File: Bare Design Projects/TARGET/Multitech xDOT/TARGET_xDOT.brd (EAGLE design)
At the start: 40.5 x 27 mm, 11 parts, among them U1 MTXDOT-EU1-A00-1

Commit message: Added LPC11u35 interface macro
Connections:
- net +3.3V_TGT renamed +3.3V
- net NRESET renamed DAP_NRESET
- net SWCLK renamed DAP_SWCLK
- net SWDIO renamed DAP_SWDIO
- net UART0_RX renamed DAP_RX
- net UART0_TX renamed DAP_TX
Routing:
- added copper zone on layer 16, net +3.3V
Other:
- board outline removed
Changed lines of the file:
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@@
 <board>
 <plain>
-<wire x1="0" y1="0" x2="40.5" y2="0" width="0" layer="20"/>
-<wire x1="40.5" y1="0" x2="40.5" y2="27" width="0" layer="20"/>
-<wire x1="40.5" y1="27" x2="0" y2="27" width="0" layer="20"/>
-<wire x1="0" y1="27" x2="0" y2="0" width="0" layer="20"/>
 <rectangle x1="31.1912" y1="11.3792" x2="40.3352" y2="22.7584" layer="41"/>
 </plain>
@@
 <attribute name="VALUE" x="35.3844" y="22.3428" size="1.016" layer="27" font="vector" ratio="12" rot="R270"/>
 </element>
-<element name="C1" library="mbed-HDK-RLCQ" package="0603" value="10uF" x="2.9845" y="15.7734" rot="R270"/>
+<element name="C1" library="mbed-HDK-RLCQ" package="0603" value="10uF" x="2.9845" y="15.7734" smashed="yes" rot="R270">
+<attribute name="NAME" x="0.7545" y="17.0434" size="1.016" layer="25" font="vector" ratio="12" rot="R270"/>
+<attribute name="VALUE" x="0.4445" y="17.0434" size="1.016" layer="27" font="vector" ratio="12" rot="R270"/>
+</element>
 <element name="C2" library="mbed-HDK-RLCQ" package="0603" value="100nF" x="2.9972" y="19.2151" rot="R90"/>
 <element name="C3" library="mbed-HDK-RLCQ" package="0402" value="6.8pF" x="29.3624" y="21.9456" smashed="yes">
@@
 <contactref element="C7" pad="1"/>
 <polygon width="0.4064" layer="1">
-<vertex x="-12.7" y="50.8"/>
-<vertex x="-12.7" y="-5.08"/>
-<vertex x="49.53" y="-5.08"/>
-<vertex x="49.53" y="50.8"/>
+<vertex x="-64" y="-42.5"/>
+<vertex x="92.5" y="-43"/>
+<vertex x="94" y="68"/>
+<vertex x="-62.5" y="68.5"/>
 </polygon>
 </signal>
@@
 <contactref element="U1" pad="P$14"/>
 </signal>
-<signal name="UART0_TX">
+<signal name="DAP_TX">
 <contactref element="U1" pad="P$15"/>
 </signal>
-<signal name="UART0_RX">
+<signal name="DAP_RX">
 <contactref element="U1" pad="P$16"/>
 </signal>
@@
 <contactref element="U1" pad="P$28"/>
 </signal>
-<signal name="SWCLK">
+<signal name="DAP_SWCLK">
 <contactref element="U1" pad="P$29"/>
 </signal>
-<signal name="SWDIO">
+<signal name="DAP_SWDIO">
 <contactref element="U1" pad="P$30"/>
 </signal>
@@
 <contactref element="U1" pad="P$32"/>
 </signal>
-<signal name="NRESET">
+<signal name="DAP_NRESET">
 <contactref element="U1" pad="P$33"/>
 </signal>
@@
 <signal name="ANT2">
 <contactref element="U1" pad="P$47"/>
-</signal>
-<signal name="+3.3V_TGT">
-<contactref element="U1" pad="P$4"/>
-<contactref element="U1" pad="P$3"/>
-<contactref element="C1" pad="1"/>
-<contactref element="C2" pad="1"/>
-<wire x1="2.9972" y1="18.3651" x2="3.0421" y2="18.41" width="0.508" layer="1"/>
-<wire x1="3.0421" y1="18.41" x2="5.334" y2="18.41" width="0.508" layer="1"/>
-<wire x1="2.9845" y1="16.6234" x2="2.9911" y2="16.63" width="0.508" layer="1"/>
-<wire x1="2.9911" y1="16.63" x2="5.334" y2="16.63" width="0.508" layer="1"/>
-<wire x1="2.9972" y1="18.3651" x2="2.9845" y2="18.3524" width="0.508" layer="1"/>
-<wire x1="2.9845" y1="18.3524" x2="2.9845" y2="16.6234" width="0.508" layer="1"/>
 </signal>
 <signal name="N$4">
@@
 <via x="39.3192" y="9.7536" extent="1-16" drill="0.6"/>
 </signal>
+<signal name="+3.3V">
+<polygon width="0.4064" layer="16">
+<vertex x="-64" y="-43"/>
+<vertex x="92" y="-43"/>
+<vertex x="92" y="68.5"/>
+<vertex x="-64" y="68.5"/>
+</polygon>
+<contactref element="U1" pad="P$4"/>
+<contactref element="U1" pad="P$3"/>
+<contactref element="C1" pad="1"/>
+<contactref element="C2" pad="1"/>
+<wire x1="2.9972" y1="18.3651" x2="3.0421" y2="18.41" width="0.508" layer="1"/>
+<wire x1="3.0421" y1="18.41" x2="5.334" y2="18.41" width="0.508" layer="1"/>
+<wire x1="2.9845" y1="16.6234" x2="2.9911" y2="16.63" width="0.508" layer="1"/>
+<wire x1="2.9911" y1="16.63" x2="5.334" y2="16.63" width="0.508" layer="1"/>
+<wire x1="2.9972" y1="18.3651" x2="2.9845" y2="18.3524" width="0.508" layer="1"/>
+<wire x1="2.9845" y1="18.3524" x2="2.9845" y2="16.6234" width="0.508" layer="1"/>
+</signal>
 </signals>

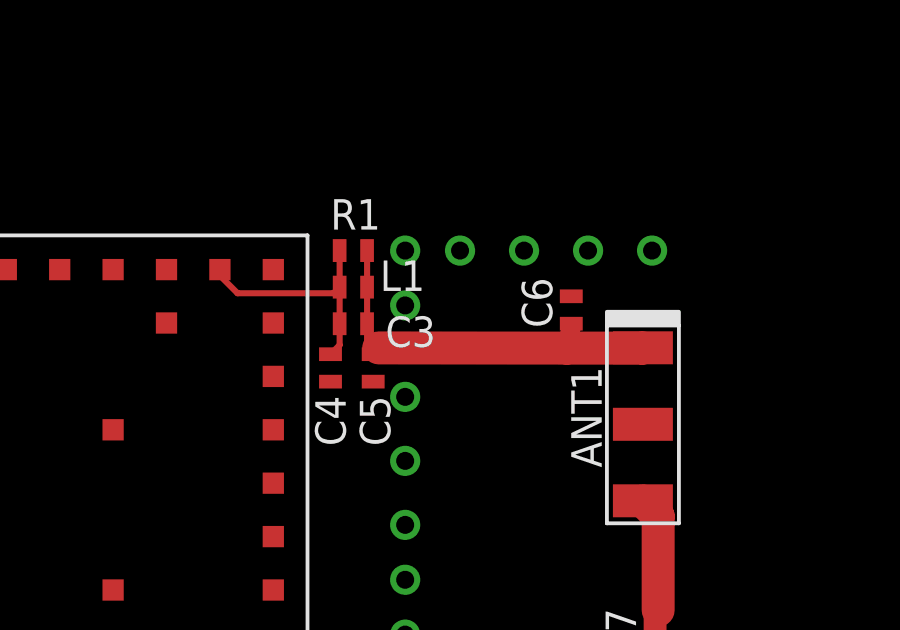
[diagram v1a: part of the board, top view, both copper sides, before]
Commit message: Updated design removed obsolete components
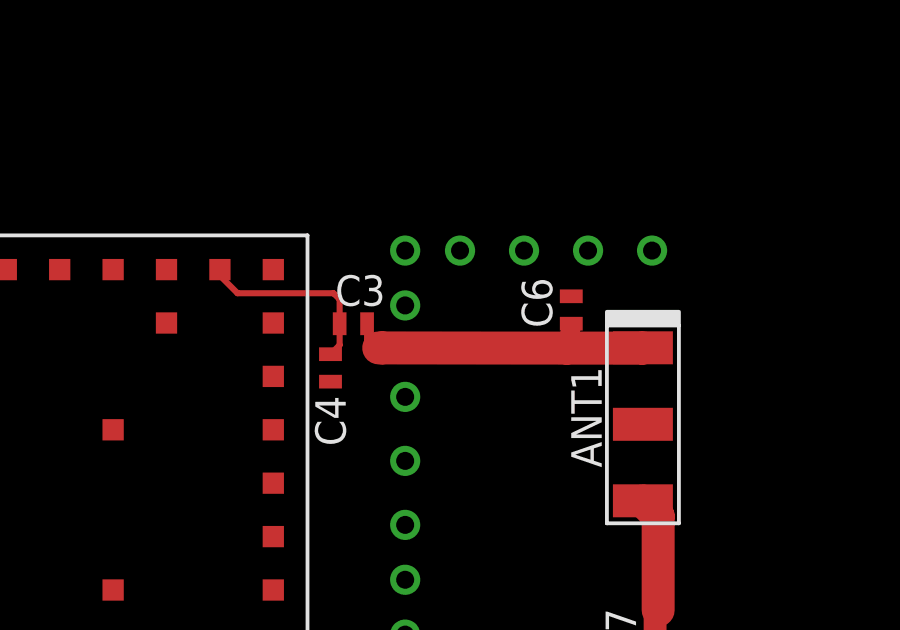
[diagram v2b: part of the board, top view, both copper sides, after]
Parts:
- removed C5: 10pF, mbed-HDK-RLCQ:0402
- removed L1: 7.5uH, mbed-HDK-RLCQ:0402
- removed R1: 0, mbed-HDK-RLCQ:0402
- C3: value 6.8pF -> 9.1pF
- C4: value 10pF -> 5.6pF
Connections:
- net DAP_NRESET renamed TGT_NRESET
- net DAP_SWCLK renamed TGT_SWCLK
- net DAP_SWDIO renamed TGT_SWDIO
- net UART1_RX renamed TGT_RX
- net UART1_TX renamed TGT_TX
- net ANT1: no longer L1.1, R1.1
- net GND: no longer C5.1
- net N$4: no longer C5.2, L1.2, R1.2
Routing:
- net N$4: track 13.7 -> 11.3 mm
- net ANT1: track 8.10 -> 6.47 mm
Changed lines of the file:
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@@
 <setting verticaltext="up"/>
 </settings>
-<grid distance="0.5" unitdist="mm" unit="mm" style="lines" multiple="1" display="no" altdistance="0.00635" altunitdist="mm" altunit="mm"/>
+<grid distance="6" unitdist="mil" unit="mil" style="lines" multiple="1" display="no" altdistance="0.00635" altunitdist="mm" altunit="mm"/>
 <layers>
 <layer number="1" name="Top" color="4" fill="1" visible="yes" active="yes"/>
@@
 </element>
 <element name="C2" library="mbed-HDK-RLCQ" package="0603" value="100nF" x="2.9972" y="19.2151" rot="R90"/>
-<element name="C3" library="mbed-HDK-RLCQ" package="0402" value="6.8pF" x="29.3624" y="21.9456" smashed="yes">
-<attribute name="NAME" x="32.1056" y="22.1869" size="1.016" layer="25" font="vector" ratio="12" rot="R180"/>
+<element name="C3" library="mbed-HDK-RLCQ" package="0402" value="9.1pF" x="29.3624" y="21.9456" smashed="yes">
+<attribute name="NAME" x="30.4292" y="23.5585" size="1.016" layer="25" font="vector" ratio="12" rot="R180"/>
 <attribute name="VALUE" x="28.0924" y="18.1356" size="1.016" layer="27" font="vector" ratio="12"/>
 </element>
-<element name="C4" library="mbed-HDK-RLCQ" package="0402" value="10pF" x="28.6004" y="20.4724" smashed="yes" rot="R90">
+<element name="C4" library="mbed-HDK-RLCQ" package="0402" value="5.6pF" x="28.6004" y="20.4724" smashed="yes" rot="R90">
 <attribute name="NAME" x="29.1084" y="17.8689" size="1.016" layer="25" font="vector" ratio="12" rot="R90"/>
 <attribute name="VALUE" x="32.4104" y="19.2024" size="1.016" layer="27" font="vector" ratio="12" rot="R90"/>
-</element>
-<element name="C5" library="mbed-HDK-RLCQ" package="0402" value="10pF" x="30.0228" y="20.4724" smashed="yes" rot="R90">
-<attribute name="NAME" x="30.5943" y="17.8689" size="1.016" layer="25" font="vector" ratio="12" rot="R90"/>
-<attribute name="VALUE" x="33.8328" y="19.2024" size="1.016" layer="27" font="vector" ratio="12" rot="R90"/>
 </element>
 <element name="C6" library="mbed-HDK-RLCQ" package="0402" value="82pF" x="36.6268" y="22.4028" smashed="yes" rot="R270">
@@
 <attribute name="NAME" x="38.7858" y="10.7823" size="1.016" layer="25" font="vector" ratio="12" rot="R90"/>
 <attribute name="VALUE" x="43.2308" y="10.2108" size="1.016" layer="27" font="vector" ratio="12" rot="R90"/>
-</element>
-<element name="L1" library="mbed-HDK-RLCQ" package="0402" value="7.5uH" x="29.3624" y="23.1648" smashed="yes">
-<attribute name="NAME" x="30.2514" y="23.0378" size="1.016" layer="25" font="vector" ratio="12"/>
-<attribute name="VALUE" x="28.0924" y="19.3548" size="1.016" layer="27" font="vector" ratio="12"/>
-</element>
-<element name="R1" library="mbed-HDK-RLCQ" package="0402" value="0" x="29.3624" y="24.384" smashed="yes">
-<attribute name="NAME" x="28.6004" y="25.0825" size="1.016" layer="25" font="vector" ratio="12"/>
-<attribute name="VALUE" x="28.0924" y="20.574" size="1.016" layer="27" font="vector" ratio="12"/>
 </element>
 <element name="U1" library="mbed-HDK-MF-MULTITECH" package="MTXDOT-EU1/NA1-A00-1" value="MTXDOT-EU1-A00-1" x="5.334" y="22.86" smashed="yes">
@@
 <contactref element="C2" pad="2"/>
 <contactref element="C4" pad="1"/>
-<contactref element="C5" pad="1"/>
 <contactref element="C6" pad="1"/>
 <contactref element="C7" pad="1"/>
@@
 <contactref element="U1" pad="P$12"/>
 </signal>
-<signal name="UART1_TX">
+<signal name="TGT_TX">
 <contactref element="U1" pad="P$13"/>
 </signal>
-<signal name="UART1_RX">
+<signal name="TGT_RX">
 <contactref element="U1" pad="P$14"/>
 </signal>
@@
 <contactref element="U1" pad="P$28"/>
 </signal>
-<signal name="DAP_SWCLK">
+<signal name="TGT_SWCLK">
 <contactref element="U1" pad="P$29"/>
 </signal>
-<signal name="DAP_SWDIO">
+<signal name="TGT_SWDIO">
 <contactref element="U1" pad="P$30"/>
 </signal>
@@
 <contactref element="U1" pad="P$32"/>
 </signal>
-<signal name="DAP_NRESET">
+<signal name="TGT_NRESET">
 <contactref element="U1" pad="P$33"/>
 </signal>
@@
 <signal name="ANT1">
 <contactref element="U1" pad="P$37"/>
-<contactref element="R1" pad="1"/>
-<contactref element="L1" pad="1"/>
 <contactref element="C4" pad="2"/>
 <contactref element="C3" pad="1"/>
-<wire x1="28.9052" y1="24.384" x2="28.9052" y2="23.1648" width="0.2032" layer="1"/>
-<wire x1="28.9052" y1="23.1648" x2="28.9052" y2="21.9456" width="0.2032" layer="1"/>
 <wire x1="24.914" y1="23.75" x2="24.914" y2="23.5492" width="0.2032" layer="1"/>
 <wire x1="24.914" y1="23.5492" x2="25.5016" y2="22.9616" width="0.2032" layer="1"/>
 <wire x1="25.5016" y1="22.9616" x2="28.702" y2="22.9616" width="0.2032" layer="1"/>
-<wire x1="28.702" y1="22.9616" x2="28.9052" y2="23.1648" width="0.2032" layer="1"/>
 <wire x1="28.6004" y1="20.9296" x2="28.9052" y2="21.2344" width="0.2032" layer="1"/>
 <wire x1="28.9052" y1="21.2344" x2="28.9052" y2="21.9456" width="0.2032" layer="1"/>
+<wire x1="28.9052" y1="21.9456" x2="28.9052" y2="22.7584" width="0.2032" layer="1"/>
+<wire x1="28.9052" y1="22.7584" x2="28.702" y2="22.9616" width="0.2032" layer="1"/>
 </signal>
 <signal name="ANT2">
@@
 <signal name="N$4">
 <contactref element="C3" pad="2"/>
-<contactref element="C5" pad="2"/>
-<contactref element="R1" pad="2"/>
-<contactref element="L1" pad="2"/>
 <contactref element="C6" pad="2"/>
 <contactref element="ANT1" pad="P$1"/>
-<wire x1="29.8196" y1="24.384" x2="29.8196" y2="23.1648" width="0.2032" layer="1"/>
-<wire x1="29.8196" y1="23.1648" x2="29.8196" y2="21.9456" width="0.2032" layer="1"/>
-<wire x1="30.0228" y1="20.9296" x2="29.8196" y2="21.1328" width="0.2032" layer="1"/>
 <wire x1="29.8196" y1="21.1328" x2="29.8196" y2="21.9456" width="0.2032" layer="1"/>
 <wire x1="39.0144" y1="21.1428" x2="39.0044" y2="21.1328" width="1.1" layer="1"/>
 <wire x1="39.0044" y1="21.1328" x2="36.4744" y2="21.1328" width="1.1" layer="1"/>
-<wire x1="36.4744" y1="21.1328" x2="30.20695" y2="21.13915" width="1.1" layer="1"/>
+<wire x1="36.4744" y1="21.1328" x2="30.32755625" y2="21.139028125" width="1.1" layer="1"/>
+<wire x1="30.32755625" y1="21.139028125" x2="30.20695" y2="21.13915" width="1.1" layer="1"/>
 <wire x1="36.6268" y1="21.9456" x2="36.6776" y2="21.8948" width="0.2032" layer="1"/>
 <wire x1="36.6776" y1="21.8948" x2="36.6776" y2="21.7424" width="0.2032" layer="1"/>
@@
 <wire x1="36.4744" y1="21.5392" x2="36.4744" y2="21.1328" width="0.508" layer="1"/>
 <wire x1="30.20695" y1="21.13915" x2="30.2387" y2="20.9296" width="0.2032" layer="1"/>
-<wire x1="30.2387" y1="20.9296" x2="30.0228" y2="20.9296" width="0.2032" layer="1"/>
+<wire x1="29.8196" y1="21.1328" x2="30.321328125" y2="21.1328" width="0.2032" layer="1"/>
+<wire x1="30.321328125" y1="21.1328" x2="30.32755625" y2="21.139028125" width="0.2032" layer="1"/>
 </signal>
 <signal name="N$1">
